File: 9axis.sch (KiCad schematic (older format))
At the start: 1 part, among them U9 MPU-9250

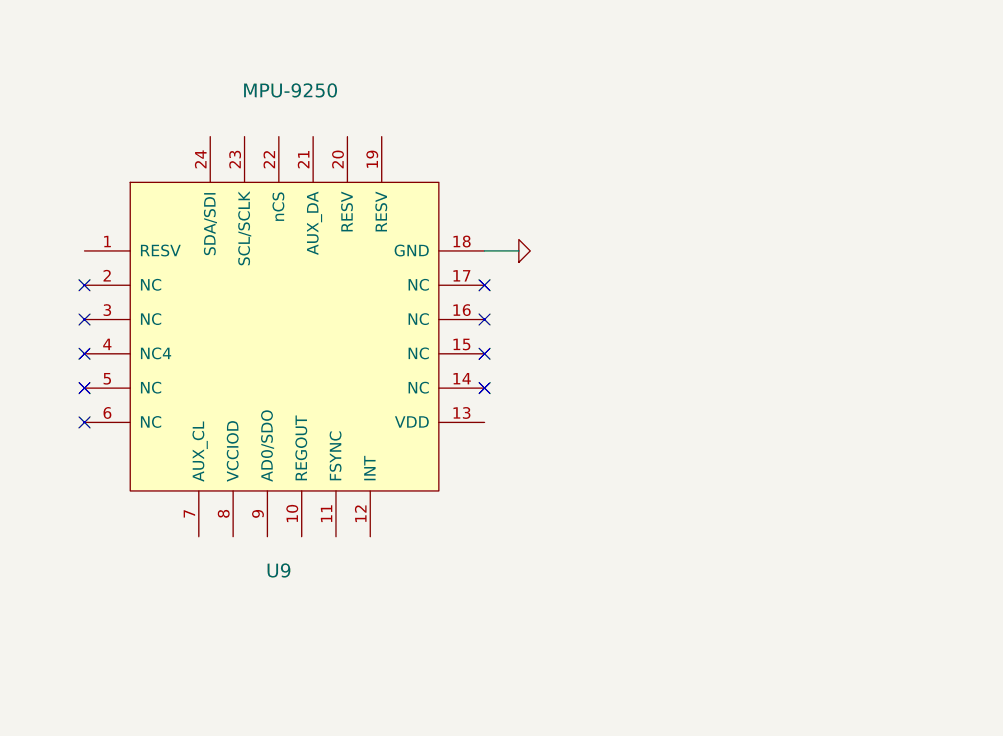
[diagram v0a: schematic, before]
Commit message: Add gps
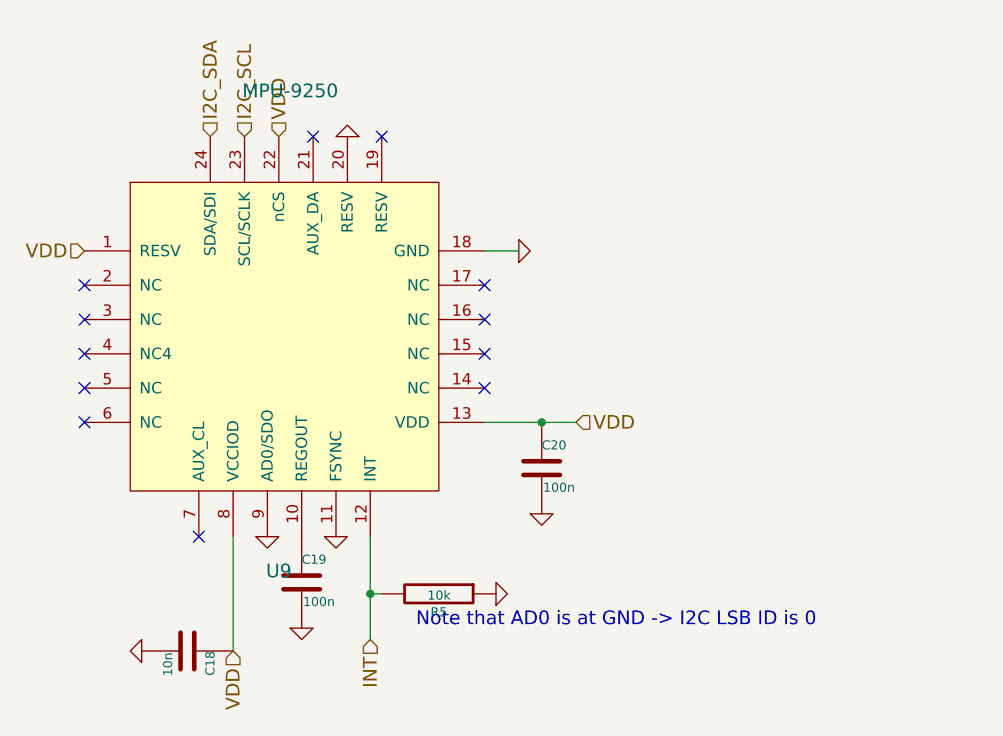
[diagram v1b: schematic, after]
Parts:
- added C18: 10n, symbol C
- added C19, C20: 100n, symbol C
- added R5: 10k, symbol R
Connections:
- net GND: now also U9.11 (FSYNC), U9.20 (RESV), U9.9 (AD0/SDO), C18.2, C19.2, C20.2, R5.1
- net VDD: now reaches U9.1 (RESV)
- net VDD: now also U9.13 (VDD), U9.22 (nCS), U9.8 (VCCIOD), C18.1, C20.1
- net at U9.10 (REGOUT): now also C19.1
- net INT: now reaches U9.12 (INT)
- net INT: now also R5.2
- net I2C_SCL: now reaches U9.23 (SCL/SCLK)
- net I2C_SDA: now reaches U9.24 (SDA/SDI)
- no-connect marks 9 -> 12
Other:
- note added: "Note that AD0 is at GND -> I2C LSB ID is 0"
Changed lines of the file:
@@
 $Descr A4 11693 8268
 encoding utf-8
-Sheet 10 10
+Sheet 10 11
 Title ""
 Date ""
@@
 NoConn ~ 6550 3500
 $Comp
-L GND #PWR16
+L GND #PWR28
 U 1 1 544656D2
 P 6700 3350
-F 0 "#PWR16" H 6700 3350 30  0001 C CNN
+F 0 "#PWR28" H 6700 3350 30  0001 C CNN
 F 1 "GND" H 6700 3280 30  0001 C CNN
 F 2 "" H 6700 3350 60  0000 C CNN
@@
 Wire Wire Line
 	6700 3350 6550 3350
+$Comp
+L C C20
+U 1 1 54610A3E
+P 6800 4300
+F 0 "C20" H 6800 4400 40  0000 L CNN
+F 1 "100n" H 6806 4215 40  0000 L CNN
+F 2 "" H 6838 4150 30  0000 C CNN
+F 3 "" H 6800 4300 60  0000 C CNN
+	1    6800 4300
+	1    0    0    -1
+$EndComp
+Text HLabel 6950 4100 2    60   Input ~ 0
+VDD
+$Comp
+L GND #PWR29
+U 1 1 54610A98
+P 6800 4500
+F 0 "#PWR29" H 6800 4500 30  0001 C CNN
+F 1 "GND" H 6800 4430 30  0001 C CNN
+F 2 "" H 6800 4500 60  0000 C CNN
+F 3 "" H 6800 4500 60  0000 C CNN
+	1    6800 4500
+	1    0    0    -1
+$EndComp
+Wire Wire Line
+	6550 4100 6950 4100
+Connection ~ 6800 4100
+Text HLabel 5350 2850 1    60   Input ~ 0
+I2C_SDA
+Text HLabel 5500 2850 1    60   Input ~ 0
+I2C_SCL
+$Comp
+L C C18
+U 1 1 54610C34
+P 5250 5100
+F 0 "C18" H 5250 5200 40  0000 L CNN
+F 1 "10n" H 5256 5015 40  0000 L CNN
+F 2 "" H 5288 4950 30  0000 C CNN
+F 3 "" H 5250 5100 60  0000 C CNN
+	1    5250 5100
+	0    1    1    0
+$EndComp
+$Comp
+L GND #PWR22
+U 1 1 54610C72
+P 5050 5100
+F 0 "#PWR22" H 5050 5100 30  0001 C CNN
+F 1 "GND" H 5050 5030 30  0001 C CNN
+F 2 "" H 5050 5100 60  0000 C CNN
+F 3 "" H 5050 5100 60  0000 C CNN
+	1    5050 5100
+	0    1    1    0
+$EndComp
+Wire Wire Line
+	5450 5100 5450 4600
+$Comp
+L C C19
+U 1 1 54610CB2
+P 5750 4800
+F 0 "C19" H 5750 4900 40  0000 L CNN
+F 1 "100n" H 5756 4715 40  0000 L CNN
+F 2 "" H 5788 4650 30  0000 C CNN
+F 3 "" H 5750 4800 60  0000 C CNN
+	1    5750 4800
+	1    0    0    -1
+$EndComp
+$Comp
+L GND #PWR24
+U 1 1 54610CDB
+P 5750 5000
+F 0 "#PWR24" H 5750 5000 30  0001 C CNN
+F 1 "GND" H 5750 4930 30  0001 C CNN
+F 2 "" H 5750 5000 60  0000 C CNN
+F 3 "" H 5750 5000 60  0000 C CNN
+	1    5750 5000
+	1    0    0    -1
+$EndComp
+Text HLabel 5450 5100 3    60   Input ~ 0
+VDD
+Text HLabel 5650 2850 1    60   Input ~ 0
+VDD
+$Comp
+L GND #PWR26
+U 1 1 54610EB1
+P 5950 2850
+F 0 "#PWR26" H 5950 2850 30  0001 C CNN
+F 1 "GND" H 5950 2780 30  0001 C CNN
+F 2 "" H 5950 2850 60  0000 C CNN
+F 3 "" H 5950 2850 60  0000 C CNN
+	1    5950 2850
+	-1   0    0    1
+$EndComp
+Text HLabel 4800 3350 0    60   Input ~ 0
+VDD
+NoConn ~ 5800 2850
+$Comp
+L GND #PWR25
+U 1 1 546111A0
+P 5900 4600
+F 0 "#PWR25" H 5900 4600 30  0001 C CNN
+F 1 "GND" H 5900 4530 30  0001 C CNN
+F 2 "" H 5900 4600 60  0000 C CNN
+F 3 "" H 5900 4600 60  0000 C CNN
+	1    5900 4600
+	1    0    0    -1
+$EndComp
+NoConn ~ 6100 2850
+NoConn ~ 5300 4600
+$Comp
+L GND #PWR23
+U 1 1 546115F0
+P 5600 4600
+F 0 "#PWR23" H 5600 4600 30  0001 C CNN
+F 1 "GND" H 5600 4530 30  0001 C CNN
+F 2 "" H 5600 4600 60  0000 C CNN
+F 3 "" H 5600 4600 60  0000 C CNN
+	1    5600 4600
+	1    0    0    -1
+$EndComp
+Text Notes 6250 5000 0    60   ~ 0
+Note that AD0 is at GND -> I2C LSB ID is 0
+$Comp
+L R R5
+U 1 1 54611795
+P 6350 4850
+F 0 "R5" V 6430 4850 40  0000 C CNN
+F 1 "10k" V 6357 4851 40  0000 C CNN
+F 2 "" V 6280 4850 30  0000 C CNN
+F 3 "" H 6350 4850 30  0000 C CNN
+	1    6350 4850
+	0    1    1    0
+$EndComp
+$Comp
+L GND #PWR27
+U 1 1 5461183E
+P 6600 4850
+F 0 "#PWR27" H 6600 4850 30  0001 C CNN
+F 1 "GND" H 6600 4780 30  0001 C CNN
+F 2 "" H 6600 4850 60  0000 C CNN
+F 3 "" H 6600 4850 60  0000 C CNN
+	1    6600 4850
+	0    -1   -1   0
+$EndComp
+Wire Wire Line
+	6100 4850 6050 4850
+Wire Wire Line
+	6050 4600 6050 5050
+Connection ~ 6050 4850
+Text HLabel 6050 5050 3    60   Input ~ 0
+INT
 $EndSCHEMATC

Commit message: More connections
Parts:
- C18, C19, C20, R5: footprint (none) -> buq2:SM0603
- U9: footprint (none) -> buq2:24QFN-3MM-3MM
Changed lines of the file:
@@
 F 0 "U9" H 5650 3050 60  0000 C CNN
 F 1 "MPU-9250" H 5700 5150 60  0000 C CNN
-F 2 "" H 5200 3900 60  0001 C CNN
+F 2 "buq2:24QFN-3MM-3MM" H 5200 3900 60  0001 C CNN
 F 3 "" H 5200 3900 60  0000 C CNN
 	1    5200 3900
@@
 NoConn ~ 6550 3500
 $Comp
-L GND #PWR28
+L GND #PWR024
 U 1 1 544656D2
 P 6700 3350
-F 0 "#PWR28" H 6700 3350 30  0001 C CNN
+F 0 "#PWR024" H 6700 3350 30  0001 C CNN
 F 1 "GND" H 6700 3280 30  0001 C CNN
 F 2 "" H 6700 3350 60  0000 C CNN
@@
 F 0 "C20" H 6800 4400 40  0000 L CNN
 F 1 "100n" H 6806 4215 40  0000 L CNN
-F 2 "" H 6838 4150 30  0000 C CNN
+F 2 "buq2:SM0603" H 6838 4150 30  0001 C CNN
 F 3 "" H 6800 4300 60  0000 C CNN
 	1    6800 4300
@@
 VDD
 $Comp
-L GND #PWR29
+L GND #PWR025
 U 1 1 54610A98
 P 6800 4500
-F 0 "#PWR29" H 6800 4500 30  0001 C CNN
+F 0 "#PWR025" H 6800 4500 30  0001 C CNN
 F 1 "GND" H 6800 4430 30  0001 C CNN
 F 2 "" H 6800 4500 60  0000 C CNN
@@
 F 0 "C18" H 5250 5200 40  0000 L CNN
 F 1 "10n" H 5256 5015 40  0000 L CNN
-F 2 "" H 5288 4950 30  0000 C CNN
+F 2 "buq2:SM0603" H 5288 4950 30  0001 C CNN
 F 3 "" H 5250 5100 60  0000 C CNN
 	1    5250 5100
@@
 $EndComp
 $Comp
-L GND #PWR22
+L GND #PWR026
 U 1 1 54610C72
 P 5050 5100
-F 0 "#PWR22" H 5050 5100 30  0001 C CNN
+F 0 "#PWR026" H 5050 5100 30  0001 C CNN
 F 1 "GND" H 5050 5030 30  0001 C CNN
 F 2 "" H 5050 5100 60  0000 C CNN
@@
 F 0 "C19" H 5750 4900 40  0000 L CNN
 F 1 "100n" H 5756 4715 40  0000 L CNN
-F 2 "" H 5788 4650 30  0000 C CNN
+F 2 "buq2:SM0603" H 5788 4650 30  0001 C CNN
 F 3 "" H 5750 4800 60  0000 C CNN
 	1    5750 4800
@@
 $EndComp
 $Comp
-L GND #PWR24
+L GND #PWR027
 U 1 1 54610CDB
 P 5750 5000
-F 0 "#PWR24" H 5750 5000 30  0001 C CNN
+F 0 "#PWR027" H 5750 5000 30  0001 C CNN
 F 1 "GND" H 5750 4930 30  0001 C CNN
 F 2 "" H 5750 5000 60  0000 C CNN
@@
 VDD
 $Comp
-L GND #PWR26
+L GND #PWR028
 U 1 1 54610EB1
 P 5950 2850
-F 0 "#PWR26" H 5950 2850 30  0001 C CNN
+F 0 "#PWR028" H 5950 2850 30  0001 C CNN
 F 1 "GND" H 5950 2780 30  0001 C CNN
 F 2 "" H 5950 2850 60  0000 C CNN
@@
 NoConn ~ 5800 2850
 $Comp
-L GND #PWR25
+L GND #PWR029
 U 1 1 546111A0
 P 5900 4600
-F 0 "#PWR25" H 5900 4600 30  0001 C CNN
+F 0 "#PWR029" H 5900 4600 30  0001 C CNN
 F 1 "GND" H 5900 4530 30  0001 C CNN
 F 2 "" H 5900 4600 60  0000 C CNN
@@
 NoConn ~ 5300 4600
 $Comp
-L GND #PWR23
+L GND #PWR030
 U 1 1 546115F0
 P 5600 4600
-F 0 "#PWR23" H 5600 4600 30  0001 C CNN
+F 0 "#PWR030" H 5600 4600 30  0001 C CNN
 F 1 "GND" H 5600 4530 30  0001 C CNN
 F 2 "" H 5600 4600 60  0000 C CNN
@@
 F 0 "R5" V 6430 4850 40  0000 C CNN
 F 1 "10k" V 6357 4851 40  0000 C CNN
-F 2 "" V 6280 4850 30  0000 C CNN
+F 2 "buq2:SM0603" V 6280 4850 30  0001 C CNN
 F 3 "" H 6350 4850 30  0000 C CNN
 	1    6350 4850
@@
 $EndComp
 $Comp
-L GND #PWR27
+L GND #PWR031
 U 1 1 5461183E
 P 6600 4850
-F 0 "#PWR27" H 6600 4850 30  0001 C CNN
+F 0 "#PWR031" H 6600 4850 30  0001 C CNN
 F 1 "GND" H 6600 4780 30  0001 C CNN
 F 2 "" H 6600 4850 60  0000 C CNN

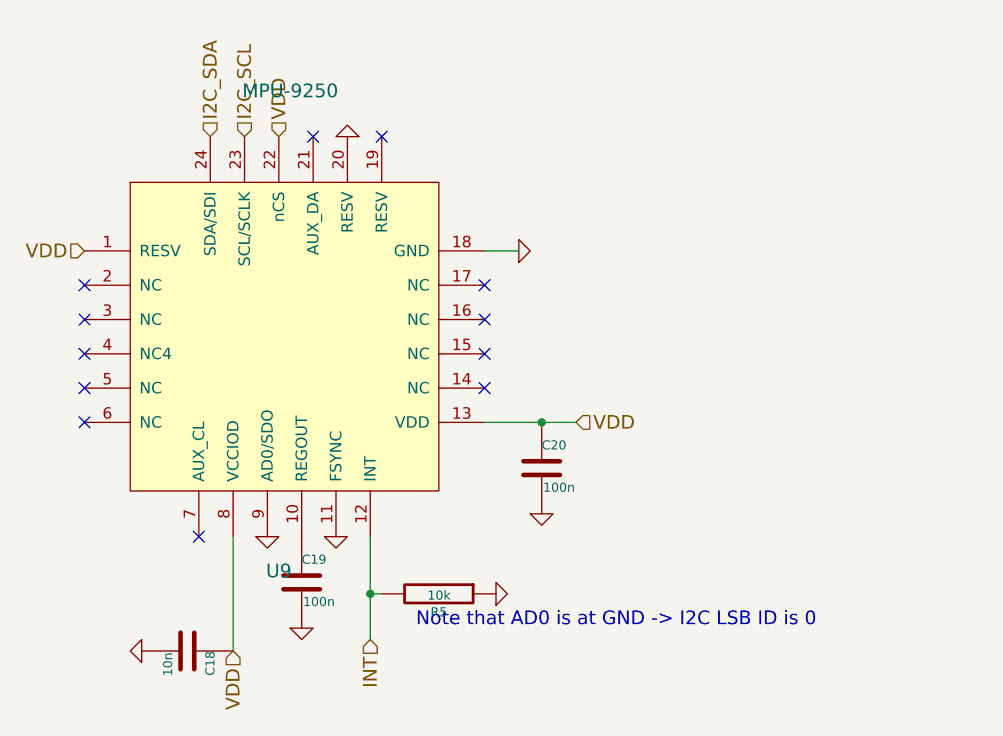
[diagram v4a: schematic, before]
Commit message: Add buttons. Fix DRC. Add antenna
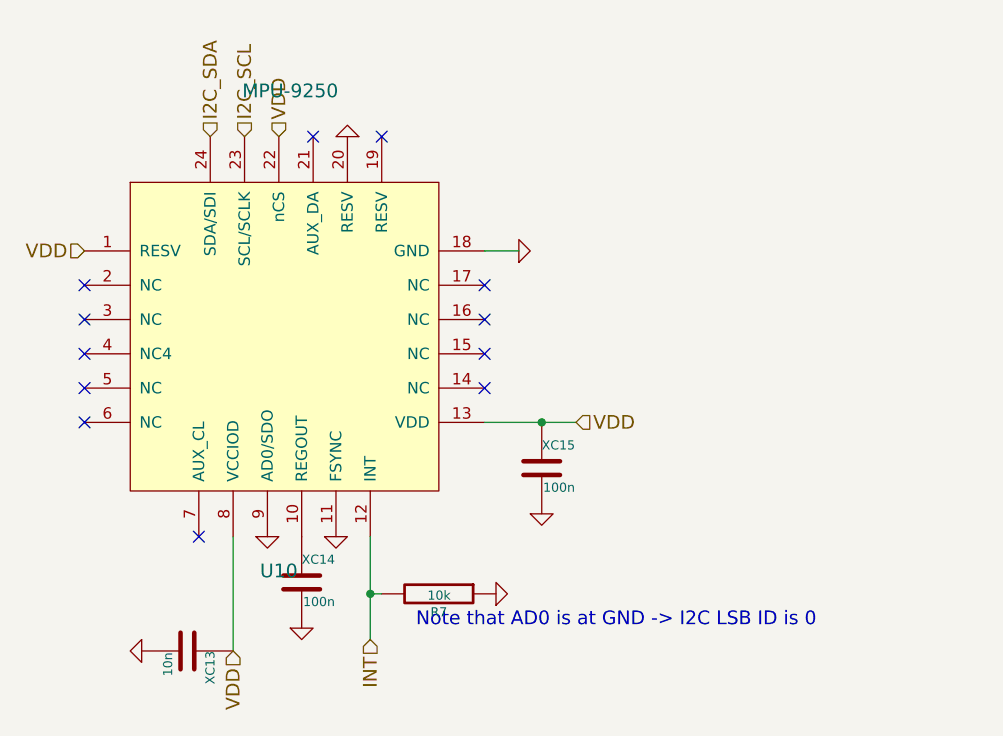
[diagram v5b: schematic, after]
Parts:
- renumbered R5 to R7, U9 to U10, C18 to XC13, C19 to XC14, C20 to XC15
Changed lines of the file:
@@
 $Descr A4 11693 8268
 encoding utf-8
-Sheet 10 13
+Sheet 10 14
 Title ""
 Date ""
@@
 $EndDescr
 $Comp
-L MPU-9250 U9
+L MPU-9250 U10
 U 1 1 544656C2
 P 5200 3900
-F 0 "U9" H 5650 3050 60  0000 C CNN
+F 0 "U10" H 5650 3050 60  0000 C CNN
 F 1 "MPU-9250" H 5700 5150 60  0000 C CNN
 F 2 "buq2:24QFN-3MM-3MM" H 5200 3900 60  0001 C CNN
@@
 NoConn ~ 6550 3500
 $Comp
-L GND #PWR025
+L GND #PWR028
 U 1 1 544656D2
 P 6700 3350
-F 0 "#PWR025" H 6700 3350 30  0001 C CNN
+F 0 "#PWR028" H 6700 3350 30  0001 C CNN
 F 1 "GND" H 6700 3280 30  0001 C CNN
 F 2 "" H 6700 3350 60  0000 C CNN
@@
 	6700 3350 6550 3350
 $Comp
-L C C20
+L C XC15
 U 1 1 54610A3E
 P 6800 4300
-F 0 "C20" H 6800 4400 40  0000 L CNN
+F 0 "XC15" H 6800 4400 40  0000 L CNN
 F 1 "100n" H 6806 4215 40  0000 L CNN
 F 2 "buq2:SM0603" H 6838 4150 30  0001 C CNN
@@
 VDD
 $Comp
-L GND #PWR026
+L GND #PWR029
 U 1 1 54610A98
 P 6800 4500
-F 0 "#PWR026" H 6800 4500 30  0001 C CNN
+F 0 "#PWR029" H 6800 4500 30  0001 C CNN
 F 1 "GND" H 6800 4430 30  0001 C CNN
 F 2 "" H 6800 4500 60  0000 C CNN
@@
 I2C_SCL
 $Comp
-L C C18
+L C XC13
 U 1 1 54610C34
 P 5250 5100
-F 0 "C18" H 5250 5200 40  0000 L CNN
+F 0 "XC13" H 5250 5200 40  0000 L CNN
 F 1 "10n" H 5256 5015 40  0000 L CNN
 F 2 "buq2:SM0603" H 5288 4950 30  0001 C CNN
@@
 $EndComp
 $Comp
-L GND #PWR027
+L GND #PWR030
 U 1 1 54610C72
 P 5050 5100
-F 0 "#PWR027" H 5050 5100 30  0001 C CNN
+F 0 "#PWR030" H 5050 5100 30  0001 C CNN
 F 1 "GND" H 5050 5030 30  0001 C CNN
 F 2 "" H 5050 5100 60  0000 C CNN
@@
 	5450 5100 5450 4600
 $Comp
-L C C19
+L C XC14
 U 1 1 54610CB2
 P 5750 4800
-F 0 "C19" H 5750 4900 40  0000 L CNN
+F 0 "XC14" H 5750 4900 40  0000 L CNN
 F 1 "100n" H 5756 4715 40  0000 L CNN
 F 2 "buq2:SM0603" H 5788 4650 30  0001 C CNN
@@
 $EndComp
 $Comp
-L GND #PWR028
+L GND #PWR031
 U 1 1 54610CDB
 P 5750 5000
-F 0 "#PWR028" H 5750 5000 30  0001 C CNN
+F 0 "#PWR031" H 5750 5000 30  0001 C CNN
 F 1 "GND" H 5750 4930 30  0001 C CNN
 F 2 "" H 5750 5000 60  0000 C CNN
@@
 VDD
 $Comp
-L GND #PWR029
+L GND #PWR032
 U 1 1 54610EB1
 P 5950 2850
-F 0 "#PWR029" H 5950 2850 30  0001 C CNN
+F 0 "#PWR032" H 5950 2850 30  0001 C CNN
 F 1 "GND" H 5950 2780 30  0001 C CNN
 F 2 "" H 5950 2850 60  0000 C CNN
@@
 NoConn ~ 5800 2850
 $Comp
-L GND #PWR030
+L GND #PWR033
 U 1 1 546111A0
 P 5900 4600
-F 0 "#PWR030" H 5900 4600 30  0001 C CNN
+F 0 "#PWR033" H 5900 4600 30  0001 C CNN
 F 1 "GND" H 5900 4530 30  0001 C CNN
 F 2 "" H 5900 4600 60  0000 C CNN
@@
 NoConn ~ 5300 4600
 $Comp
-L GND #PWR031
+L GND #PWR034
 U 1 1 546115F0
 P 5600 4600
-F 0 "#PWR031" H 5600 4600 30  0001 C CNN
+F 0 "#PWR034" H 5600 4600 30  0001 C CNN
 F 1 "GND" H 5600 4530 30  0001 C CNN
 F 2 "" H 5600 4600 60  0000 C CNN
@@
 Note that AD0 is at GND -> I2C LSB ID is 0
 $Comp
-L R R5
+L R R7
 U 1 1 54611795
 P 6350 4850
-F 0 "R5" V 6430 4850 40  0000 C CNN
+F 0 "R7" V 6430 4850 40  0000 C CNN
 F 1 "10k" V 6357 4851 40  0000 C CNN
 F 2 "buq2:SM0603" V 6280 4850 30  0001 C CNN
@@
 $EndComp
 $Comp
-L GND #PWR032
+L GND #PWR035
 U 1 1 5461183E
 P 6600 4850
-F 0 "#PWR032" H 6600 4850 30  0001 C CNN
+F 0 "#PWR035" H 6600 4850 30  0001 C CNN
 F 1 "GND" H 6600 4780 30  0001 C CNN
 F 2 "" H 6600 4850 60  0000 C CNN
